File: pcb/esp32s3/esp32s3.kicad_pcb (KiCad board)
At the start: 4 copper layers, 59.7 x 58.9 mm, 82 parts, among them J1 USB_C_Receptacle_USB2.0_14P, J2 Battery, J3 GPS_ANT, J4 Conn_Coaxial, J5 Conn_01x40_Socket, Q1_Xtal1 32.0MHz, Q3 DMG1012T, SW1 BOOT, SW2 PTS815 SJM 250 SMTR LFS, U1 ESP32-S3N8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

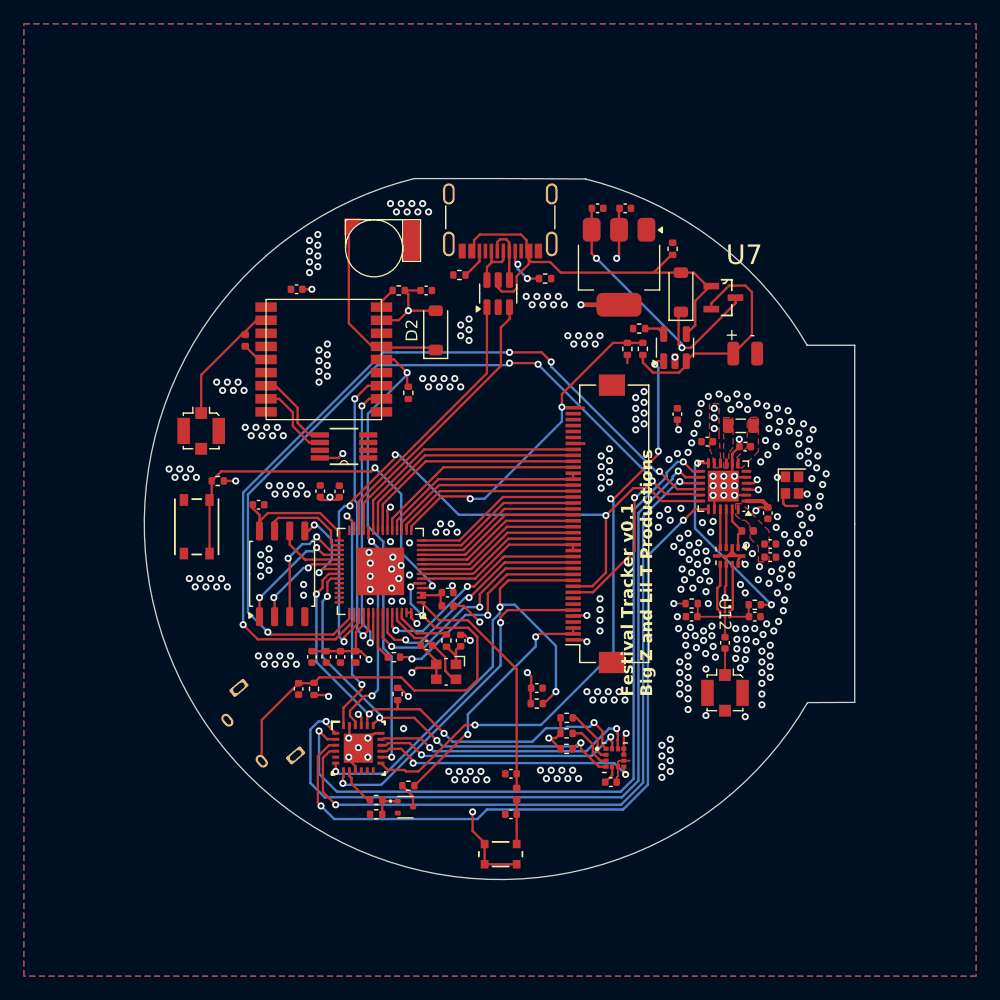
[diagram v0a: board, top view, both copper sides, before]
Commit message: added "stm32h7" new pcb and docs
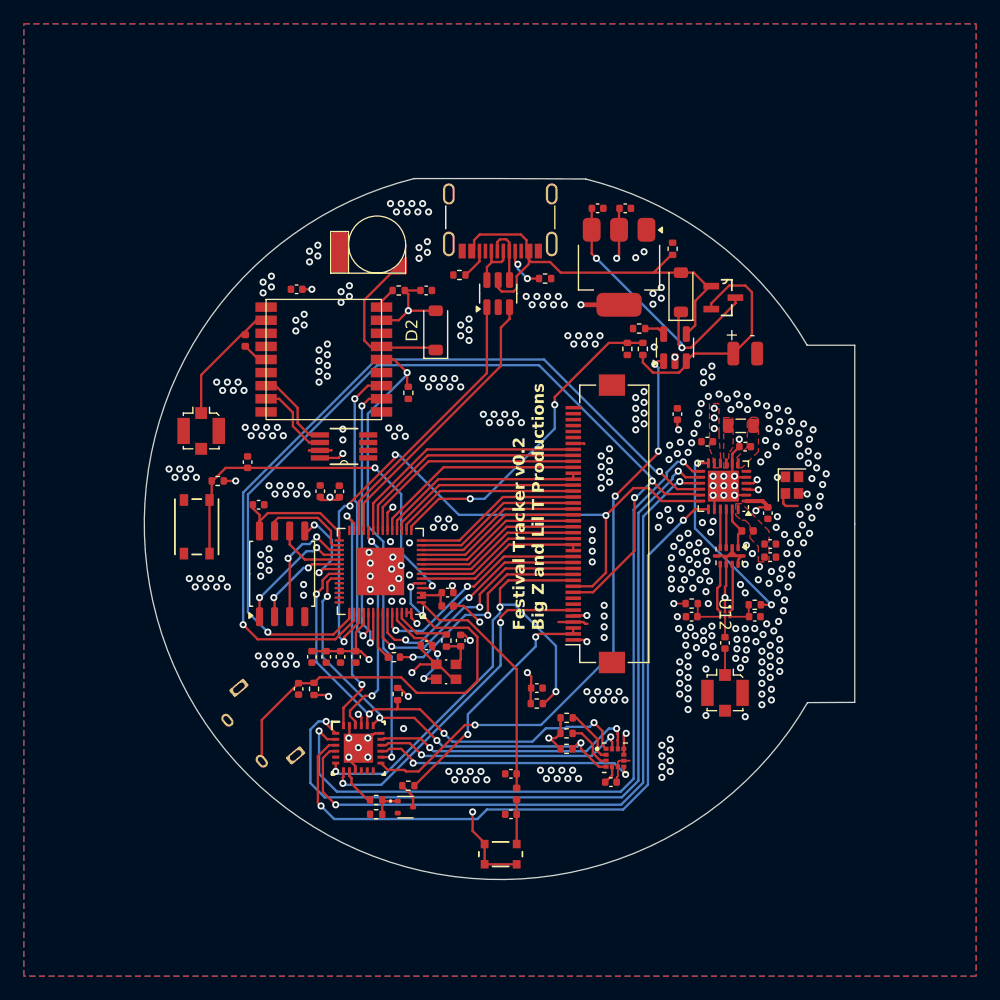
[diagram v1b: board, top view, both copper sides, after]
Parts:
- added C26: 100nF, Capacitor_SMD:C_0402_1005Metric, F.Cu at (108.8, 66.8)
- X1: footprint Crystal:Crystal_SMD_Abracon_ABM10-4Pin_2.5x2.0mm -> custom_comps:XTAL_ABM10-40.000MHZ-D30-T3
- moved BT1 0.40 mm to (119.7, 48.5), turned to -90 degrees
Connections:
- X1 pad 3: GND -> XTAL_N
- X1 pad 4: XTAL_N -> GND
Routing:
- net GND: track 50.6 -> 55.0 mm, vias 354 -> 407
- net Net-(ATGM336H1-VBAT): track 16.6 -> 14.0 mm
- net XTAL_N: track 8.34 -> 9.11 mm, vias 0 -> 2
- net MISO: track 70.5 -> 69.8 mm, vias 4 -> 2
- net Net-(C1-Pad1): track 3.71 -> 2.98 mm
- net MOSI: track 80.7 -> 80.5 mm, vias 5 -> 3
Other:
- board text added: "3"
- board text added: ":"
- board text added: "Festival Tracker v0.2 Big Z and Lil T Productions"
- board text added: "please just show up on the computer. make the little noise and let me program you. you know you want it. it's not even that hard. communicate over usb like a good little board."
- board text removed: ": 3"
- board text removed: "Festival Tracker v0.1 Big Z and Lil T Productions"
